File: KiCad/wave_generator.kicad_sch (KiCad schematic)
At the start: 10 parts, among them U4 MCP6002-xP

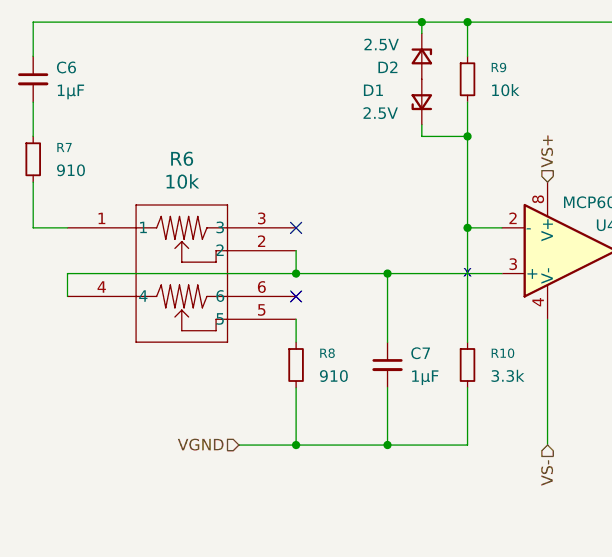
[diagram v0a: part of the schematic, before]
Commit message: changed resistance on schematic for minimum reisstance of 20kOhm
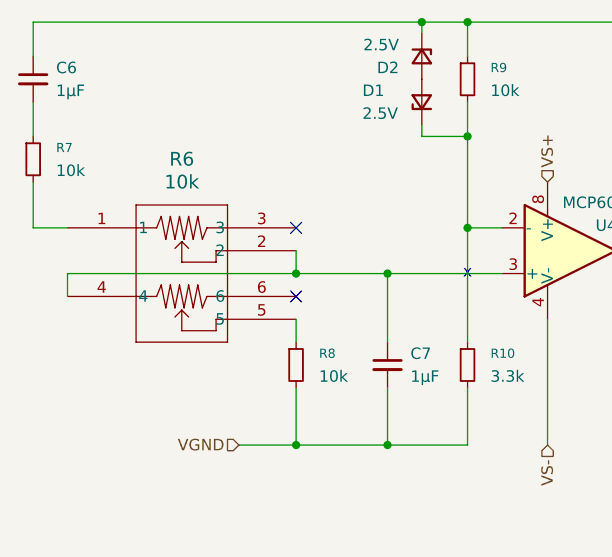
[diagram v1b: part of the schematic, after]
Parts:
- R7, R8: value 910 -> 10k
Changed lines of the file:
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@@
 			)
 		)
-		(property "Value" "910"
+		(property "Value" "10k"
 			(at 91.44 63.4999 0)
 			(effects
@@
 			)
 		)
-		(property "Value" "910"
+		(property "Value" "10k"
 			(at 62.23 40.6399 0)
 			(effects

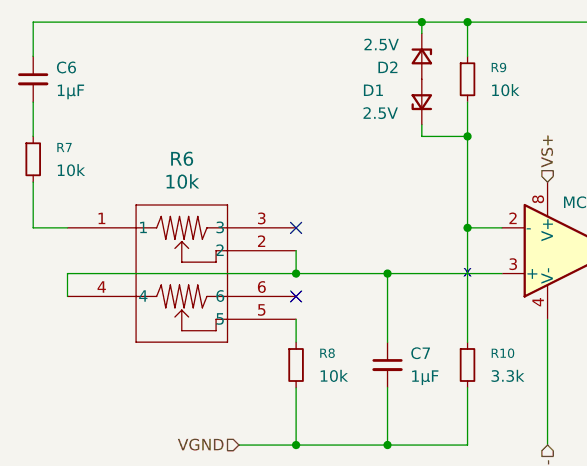
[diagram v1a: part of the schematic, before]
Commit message: changed resistor values after testing
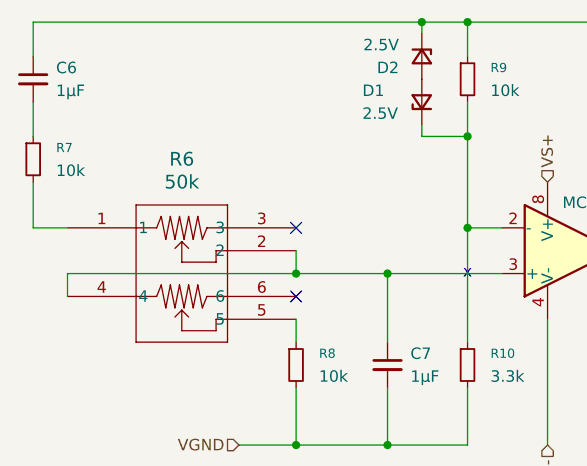
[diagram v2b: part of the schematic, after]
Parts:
- R6: value 10k -> 50k
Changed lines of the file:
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@@
 			)
 		)
-		(property "Value" "10k"
+		(property "Value" "50k"
 			(at 76.2 41.91 0)
 			(effects

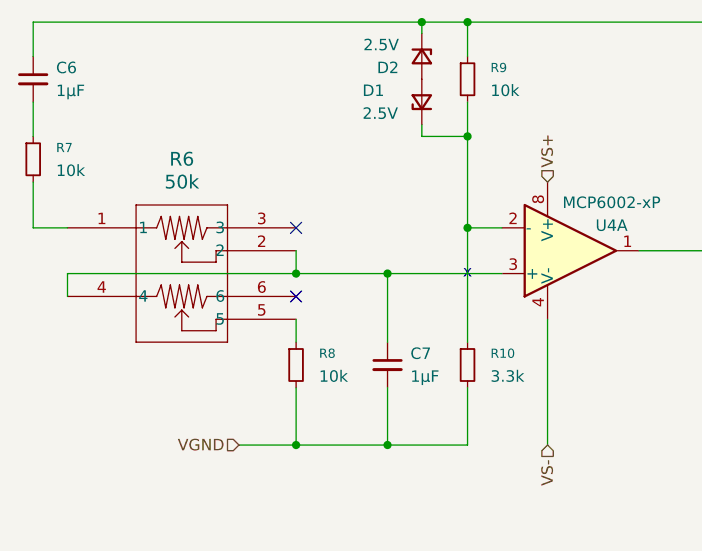
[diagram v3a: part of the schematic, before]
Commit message: Swapped mcp6002 rail splitter for TI TLE2426xP
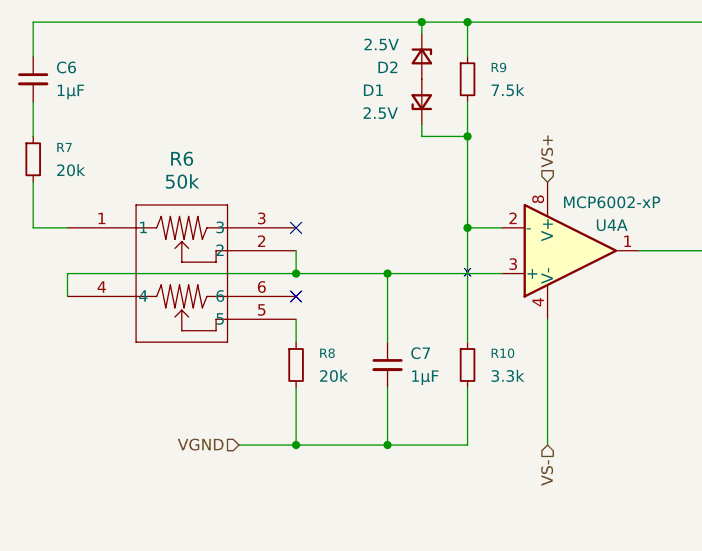
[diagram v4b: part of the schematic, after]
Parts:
- R7, R8: value 10k -> 20k
- R9: value 10k -> 7.5k
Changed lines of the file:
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@@
 			"ADYAYwBTAGEARAB0AGEAcQAzAFQAZgBSAGkAZQBiAFoAUQBPADcANQA3AFQAOABtAHAAWQBQAHAA"
 			"dgBTADMAYwBKAEUAUABuAEwAUQBRAFcAUQBGAG0ARgBZAGYATQBQACsAVwBVAFUAMgBLAHgAbQBI"
-			"AFIAeABvAEsANgB1ADYAMwByAGYAdgBuADIAcAB3ADkAdgBlAG8AQwAzAEYAYg=="
+			"AFIAeABvAEsANgB1ADYAMwByAGYAdgBuADIAcAB3ADkAdgBlAG8AQwAzAEYAYgAAAAAAAABXAABX"
+			"BOzyAMDOo47CAQAAIHzXY8IBAAByAGYAXwBnAHAAcwA6AHUAYgBsAG8AeABfAHoAbwBlAF8AbQA4"
+			"AAAAAAAAAAAAAAAAAAAAAAAAAG5t8KAApgCAgBhQisIBAADAKVCKwgEAANAFUIrCAQAA4PhPisIB"
+			"AAAQLlCKwgEAANAcUIrCAQAAAAAAAAAAAABybeygAKcAgGQAYwAvAGQAYwAgAGMAbwBuAHYAZQBy"
+			"AHQAZQByACAAcwBpAG4AZwBsAGUAAAAAAAgAAAAAAAAAdm3ooACoAIBkAGMALwBkAGMAIABjAG8A"
+			"bgB2AGUAcgB0AGUAcgAgAHMAaQBuAGcAbABlAAAAAAAAAAAAAAAAAHpt5KAAqQCAZABjAC8AZABj"
+			"ACAAYwBvAG4AdgBlAHIAdABlAHIAIABkAHUAYQBsAAAASCfCAQAACAAAAAAAAAB+beCgAKoAgGQA"
+			"YwAvAGQAYwAgAGMAbwBuAHYAZQByAHQAZQByACAAZAB1AGEAbAAAAGUAAAAAAAgAAAAAAAAAAm2c"
+			"oACrAIBzAGkAbgBnAGwAZQAgAGMAbwBtAHAAYQByAGEAdABvAHIAAAAAAAAAAAAAAAAAAAAIAAAA"
+			"AAAAAAZtmKAArACAYwBtAHAAIABvAHAAZQBuACAAYwBvAGwAbABlAGMAdABvAHIAAAAAAPC+CSbC"
+			"AQAAAAAAAAAAAAAKbZSgAK0AgGQAYwAvAGQAYwAgAGMAbwBuAHYAZQByAHQAZQByACAAZAB1AGEA"
+			"bAAAAGUAAAAAAAgAAAAAAAAADm2QoACuAIBkAGMALwBkAGMAIABjAG8AbgB2AGUAcgB0AGUAcgAg"
+			"AHMAaQBuAGcAbABlAAAAAAAIAAAAAAAAABJtjKAArwCAOAAtAGkAbgBwAHUAdAAgAE8AUgAvAE4A"
+			"TwBSACAAZwBhAHQAZQAAAAAAAAAAAAAACAAAAAAAAAAWbYigALAAgGQAYwAvAGQAYwAgAGMAbwBu"
+			"AHYAZQByAHQAZQByACAAcwBpAG4AZwBsAGUAAAAAAAgAAAAAAAAAGm2EoACxAIBkAGMALwBkAGMA"
+			"IABjAG8AbgB2AGUAcgB0AGUAcgAgAHMAaQBuAGcAbABlAAAAAAAIAAAAAAAAAB5tgKAAsgCAZABj"
+			"AC8AZABjACAAYwBvAG4AdgBlAHIAdABlAHIAIABzAGkAbgBnAGwAZQAAAAAAAAAAAAAAAAAibbyg"
+			"ALMAgGQAYwAvAGQAYwAgAGMAbwBuAHYAZQByAHQAZQByACAAZAB1AGEAbAAAAAAAAAAAAAgAAAAA"
+			"AAAAJm24oAC0AIDwZ02KwgEAAGCXTYrCAQAAoHpNisIBAABgaU2KwgEAABCqTQ=="
 		)
 	)
@@
 			)
 		)
-		(property "Value" "10k"
+		(property "Value" "7.5k"
 			(at 110.49 31.7499 0)
 			(effects
@@
 			)
 		)
-		(property "Value" "10k"
+		(property "Value" "20k"
 			(at 91.44 63.4999 0)
 			(effects
@@
 			)
 		)
-		(property "Value" "10k"
+		(property "Value" "20k"
 			(at 62.23 40.6399 0)
 			(effects

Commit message: started edited pcb layout
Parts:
- C6, C7: footprint (none) -> Capacitor_SMD:C_0201_0603Metric
- D1, D2: footprint (none) -> Diode_SMD:D_0402_1005Metric
- R10, R7, R9: footprint (none) -> Resistor_SMD:R_0201_0603Metric
- R6: footprint PRS12R-4_BRN -> PRS12R_4025K_103B1:PRS12R-4_BRN
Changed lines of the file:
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@@
 			)
 		)
-		(property "Footprint" "PRS12R-4_BRN"
+		(property "Footprint" "PRS12R_4025K_103B1:PRS12R-4_BRN"
 			(at 63.5 46.99 0)
 			(effects
@@
 			)
 		)
-		(property "Footprint" ""
+		(property "Footprint" "Diode_SMD:D_0402_1005Metric"
 			(at 102.87 27.94 90)
 			(effects
@@
 			)
 		)
-		(property "Footprint" ""
+		(property "Footprint" "Capacitor_SMD:C_0201_0603Metric"
 			(at 99.06 62.23 0)
 			(effects
@@
 			)
 		)
-		(property "Footprint" ""
+		(property "Footprint" "Resistor_SMD:R_0201_0603Metric"
 			(at 107.95 30.48 0)
 			(effects
@@
 			)
 		)
-		(property "Footprint" ""
+		(property "Footprint" "Resistor_SMD:R_0201_0603Metric"
 			(at 107.95 62.23 0)
 			(effects
@@
 			)
 		)
-		(property "Footprint" ""
+		(property "Footprint" "Capacitor_SMD:C_0201_0603Metric"
 			(at 59.69 30.48 0)
 			(effects
@@
 			)
 		)
-		(property "Footprint" ""
+		(property "Footprint" "Resistor_SMD:R_0201_0603Metric"
 			(at 59.69 39.37 0)
 			(effects
@@
 			)
 		)
-		(property "Footprint" ""
+		(property "Footprint" "Diode_SMD:D_0402_1005Metric"
 			(at 102.87 33.02 90)
 			(effects

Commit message: updated footprint to be all THT, battery holder still not there
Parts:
- C6, C7: footprint Capacitor_SMD:C_0201_0603Metric -> Capacitor_THT:C_Disc_D5.0mm_W2.5mm_P2.50mm
- D1: footprint Diode_SMD:D_0402_1005Metric -> Diode_THT:D_5W_P5.08mm_Vertical_AnodeUp
- D2: footprint Diode_SMD:D_0402_1005Metric -> Diode_THT:D_5W_P5.08mm_Vertical_KathodeUp
- R10, R7, R9: footprint Resistor_SMD:R_0201_0603Metric -> Resistor_THT:R_Axial_DIN0204_L3.6mm_D1.6mm_P2.54mm_Vertical
- R8: footprint (none) -> Resistor_THT:R_Axial_DIN0204_L3.6mm_D1.6mm_P2.54mm_Vertical
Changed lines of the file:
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@@
 			)
 		)
-		(property "Footprint" "Diode_SMD:D_0402_1005Metric"
+		(property "Footprint" "Diode_THT:D_5W_P5.08mm_Vertical_KathodeUp"
 			(at 102.87 27.94 90)
 			(effects
@@
 			)
 		)
-		(property "Footprint" "Capacitor_SMD:C_0201_0603Metric"
+		(property "Footprint" "Capacitor_THT:C_Disc_D5.0mm_W2.5mm_P2.50mm"
 			(at 99.06 62.23 0)
 			(effects
@@
 			)
 		)
-		(property "Footprint" "Resistor_SMD:R_0201_0603Metric"
+		(property "Footprint" "Resistor_THT:R_Axial_DIN0204_L3.6mm_D1.6mm_P2.54mm_Vertical"
 			(at 107.95 30.48 0)
 			(effects
@@
 			)
 		)
-		(property "Footprint" ""
+		(property "Footprint" "Resistor_THT:R_Axial_DIN0204_L3.6mm_D1.6mm_P2.54mm_Vertical"
 			(at 88.9 62.23 0)
 			(effects
@@
 			)
 		)
-		(property "Footprint" "Resistor_SMD:R_0201_0603Metric"
+		(property "Footprint" "Resistor_THT:R_Axial_DIN0204_L3.6mm_D1.6mm_P2.54mm_Vertical"
 			(at 107.95 62.23 0)
 			(effects
@@
 			)
 		)
-		(property "Footprint" "Capacitor_SMD:C_0201_0603Metric"
+		(property "Footprint" "Capacitor_THT:C_Disc_D5.0mm_W2.5mm_P2.50mm"
 			(at 59.69 30.48 0)
 			(effects
@@
 			)
 		)
-		(property "Footprint" "Resistor_SMD:R_0201_0603Metric"
+		(property "Footprint" "Resistor_THT:R_Axial_DIN0204_L3.6mm_D1.6mm_P2.54mm_Vertical"
 			(at 59.69 39.37 0)
 			(effects
@@
 			)
 		)
-		(property "Footprint" "Diode_SMD:D_0402_1005Metric"
+		(property "Footprint" "Diode_THT:D_5W_P5.08mm_Vertical_AnodeUp"
 			(at 102.87 33.02 90)
 			(effects
